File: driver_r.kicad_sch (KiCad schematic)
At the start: 38 parts, among them Q2 PNP, Q5 IRFZ48N, Q6 IRFZ48N, Q7 IRFZ48N, Q8 IRFZ48N, U3 74HC14, U5 TD340I, U6 TS922I, U8 74HC14

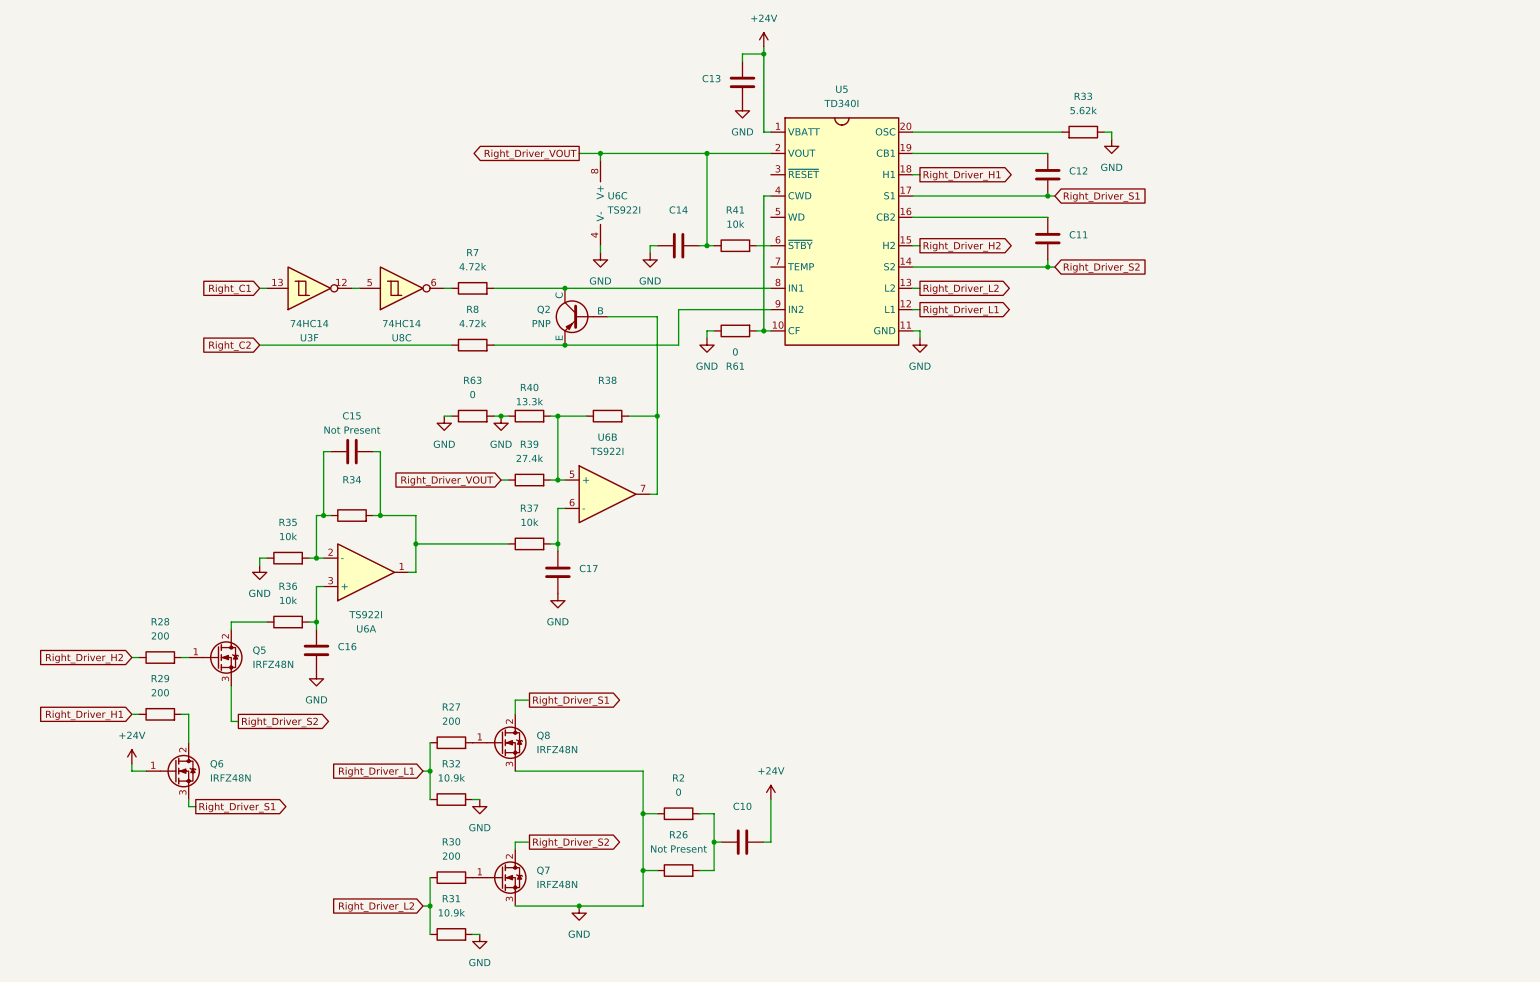
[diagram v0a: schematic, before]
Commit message: Simplified sheet tree; fixed all labels
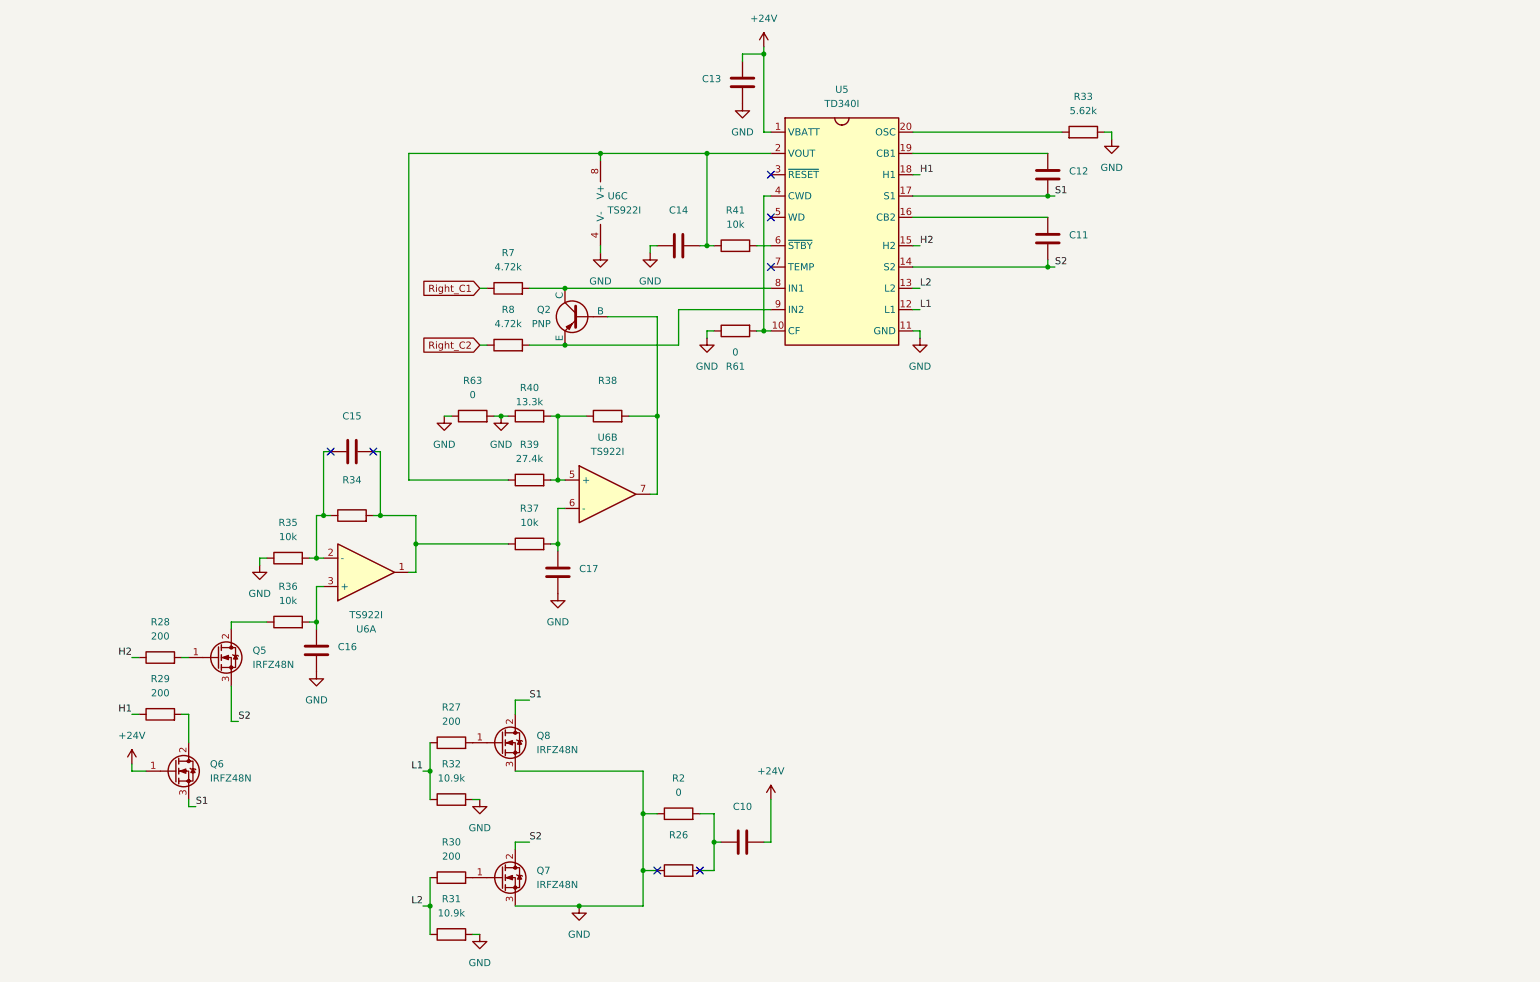
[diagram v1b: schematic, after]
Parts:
- removed U3: 74HC14, Package_DIP:DIP-14_W7.62mm_SMDSocket_SmallPads, symbol 74xx:74HC14
- removed U8: 74HC14, symbol 74xx:74HC14
- C15, R26: value Not Present -> (none)
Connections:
- net Right_C1: now also R7.1
- net Right_Driver_H1 renamed H1
- net Right_Driver_H2 renamed H2
- net Right_Driver_L1 renamed L1
- net Right_Driver_L2 renamed L2
- net Right_Driver_S1 renamed S1
- net Right_Driver_S2 renamed S2
- net Right_Driver_VOUT: no longer names the net of C14.1, R39.1, R41.1, U5.2 (VOUT), U6.8 (V+)
- no-connect marks 0 -> 7
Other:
- company: (none) -> CC0-1.0 License
- title: (none) -> Right Driver
- moved on the sheet: R7, R8

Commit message: Add IRF5303 symbol and datasheet Add power distribution and generation Fix several issues related to power distribution Rework unused buffers Fix grounding and pull-downs
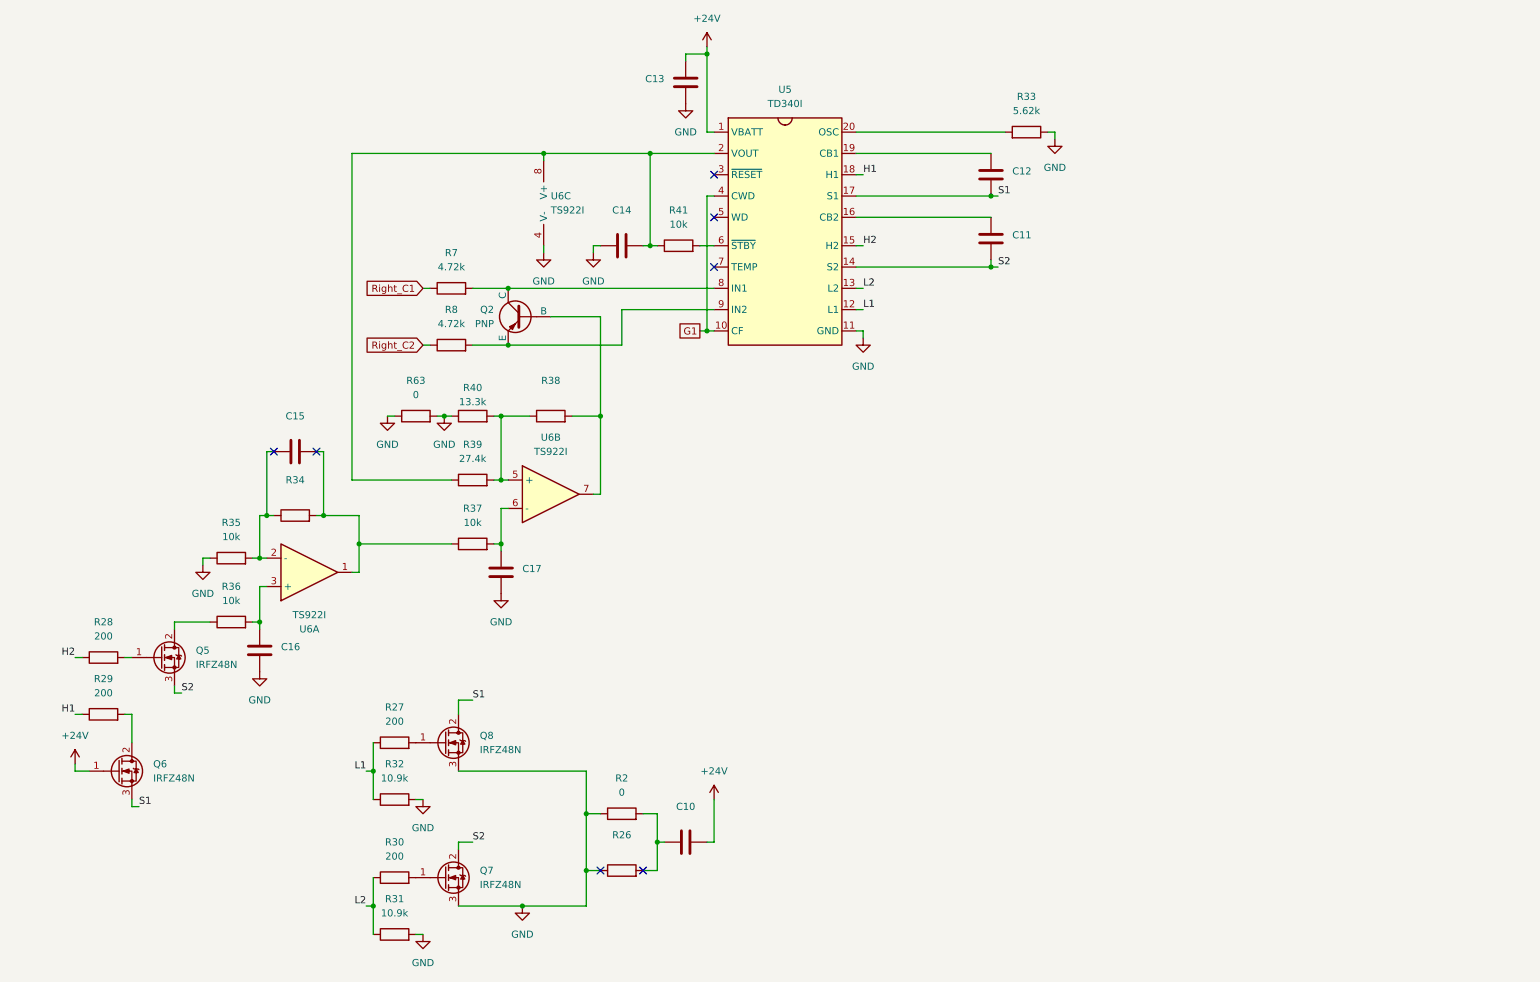
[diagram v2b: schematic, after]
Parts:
- removed R61: 0, symbol Device:R
- C15, R26: value (none) -> ~
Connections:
- net G1: now reaches U5.10 (CF), U5.4 (CWD)
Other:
- moved on the sheet: C10, C11, C12, C13, C14, C15, C16, C17, Q2, Q5, Q6, Q7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

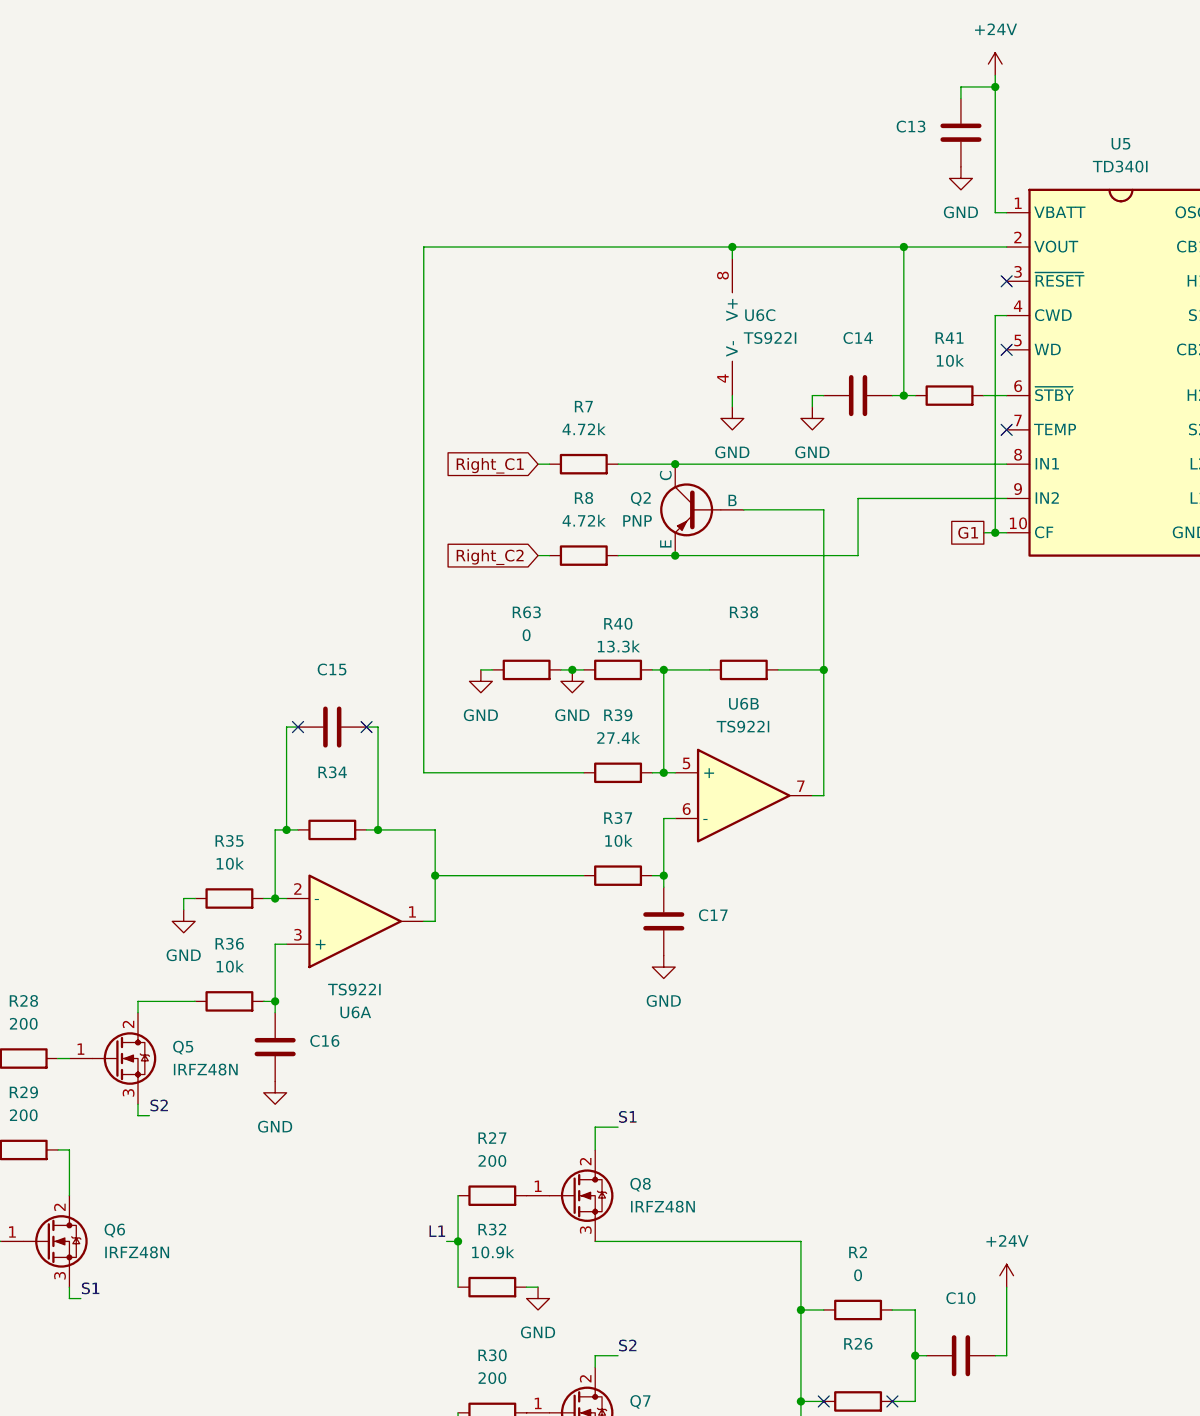
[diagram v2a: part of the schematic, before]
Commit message: Fix main power distribution (+24V->+VBATT) and generation Use standard form for amplifiers Update date
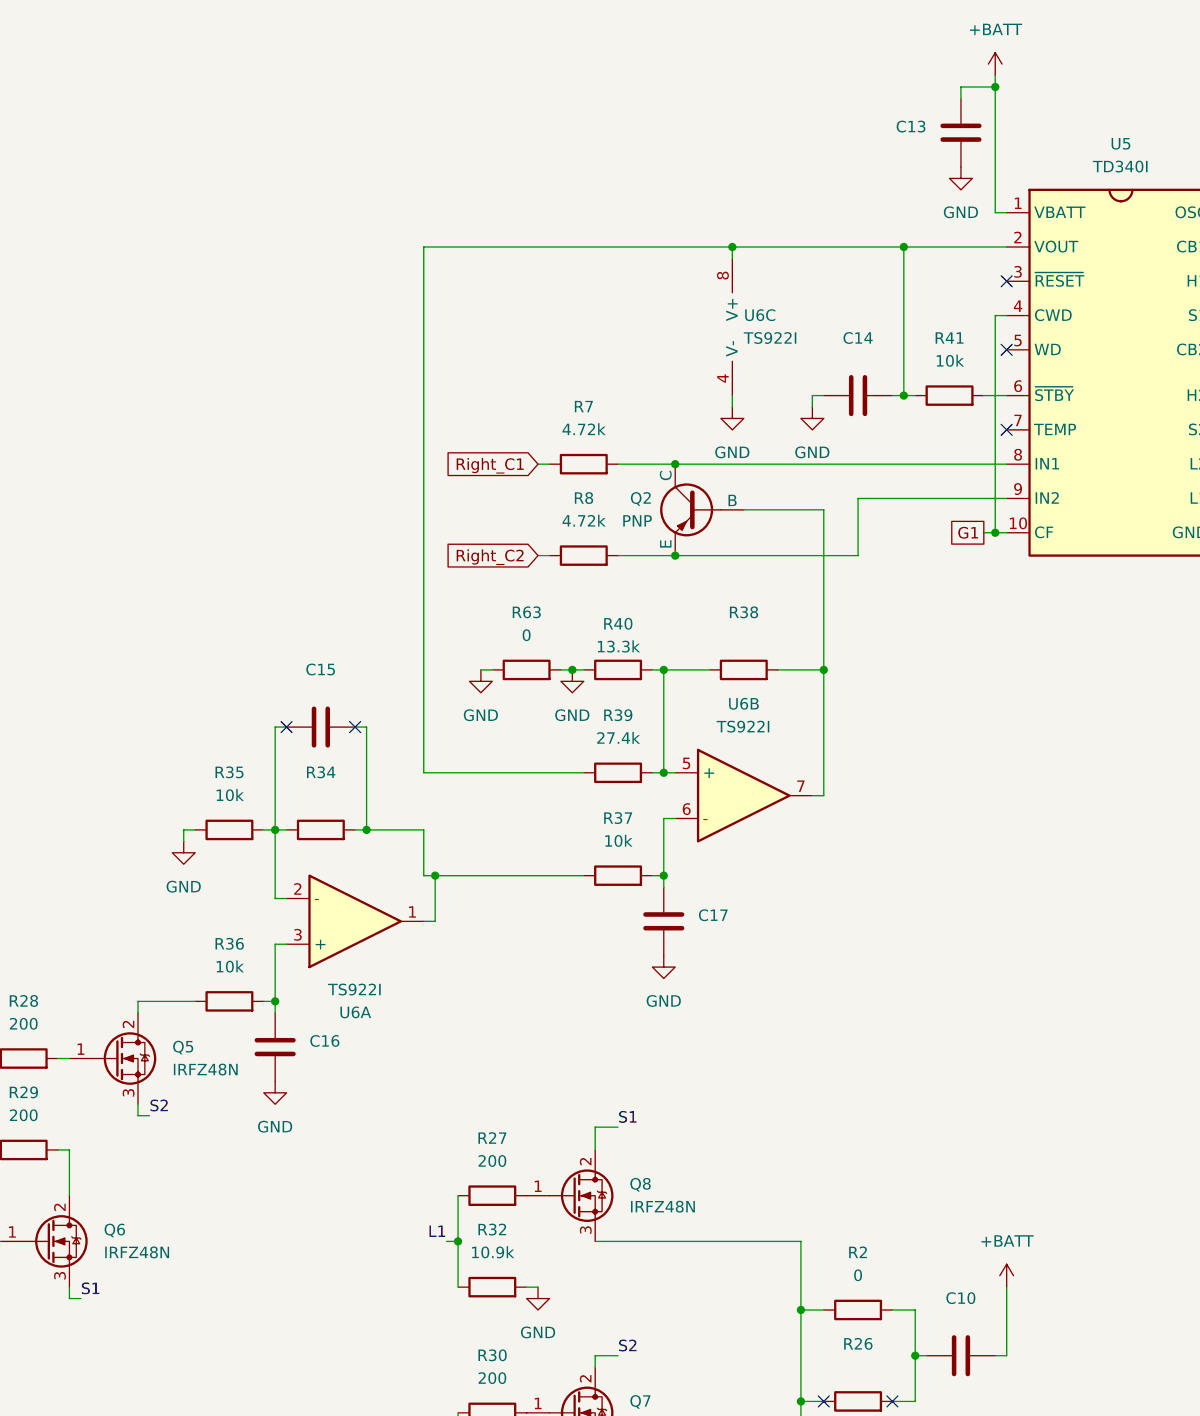
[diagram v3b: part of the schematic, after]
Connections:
- net +24V: no longer C10.2, C13.1, U5.1 (VBATT)
- new net +BATT: C10.2, C13.1, U5.1 (VBATT)
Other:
- moved on the sheet: C15, R34, R35
